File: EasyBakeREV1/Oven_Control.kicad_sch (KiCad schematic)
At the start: 11 parts, among them U6 SQ2310ES_SOT23, U9 SN74LVC1G32

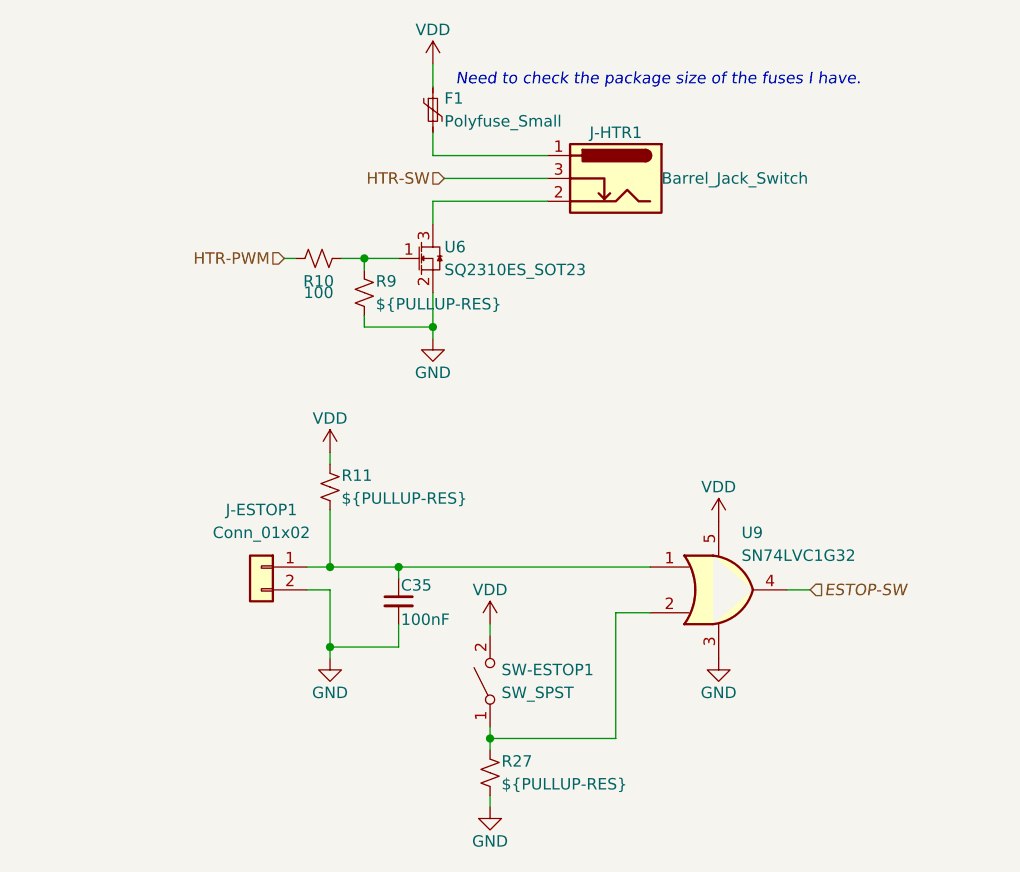
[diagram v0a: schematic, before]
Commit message: REV3 - Reorganize MC pinouts and add LED driver (WIP)
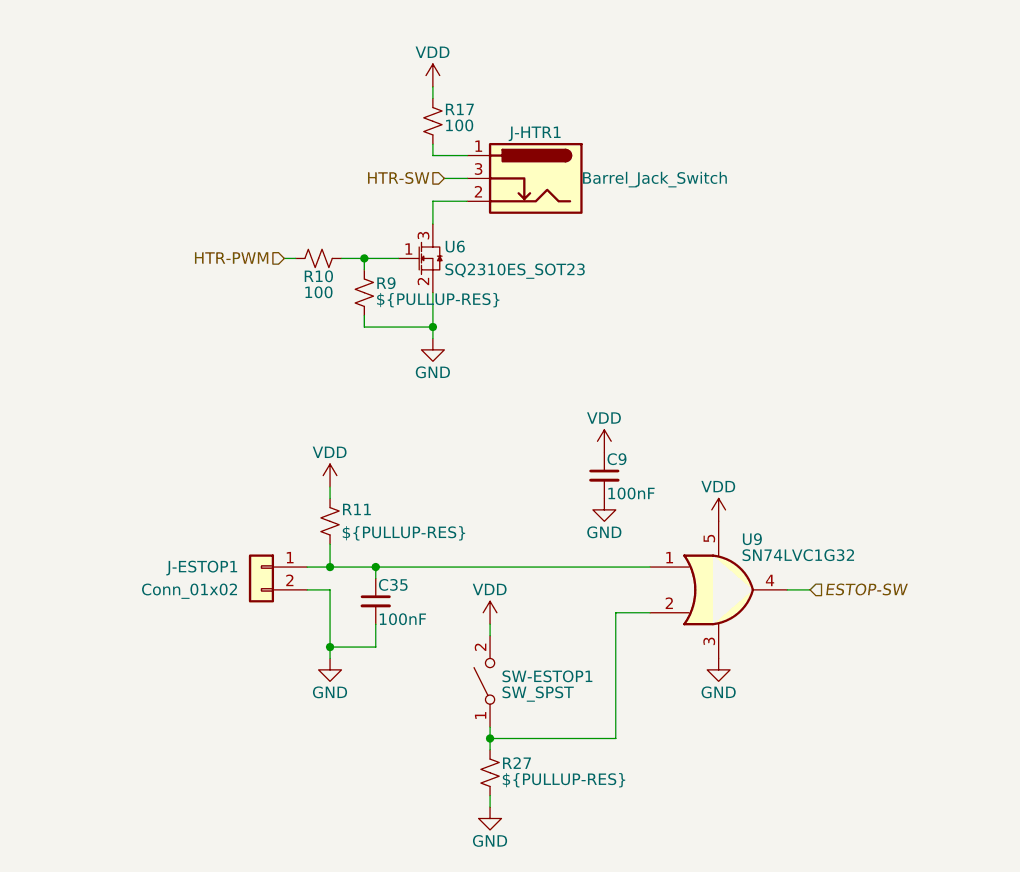
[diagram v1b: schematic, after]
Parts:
- removed F1: Polyfuse_Small, Fuse:Fuse_1210_3225Metric_Pad1.42x2.65mm_HandSolder, symbol Device:Polyfuse_Small
- added C9: 100nF, Capacitor_SMD:C_0603_1608Metric, symbol Device:C_Small
- added R17: 100, Resistor_SMD:R_0603_1608Metric, symbol Device:R_Small_US
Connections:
- net GND: now also C9.2
- net VDD: now also C9.1, R17.2
- net at J-HTR1.1: now also R17.1
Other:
- note removed: "Need to check the package size of the fuses I have."
- moved on the sheet: C35, J-HTR1, R11

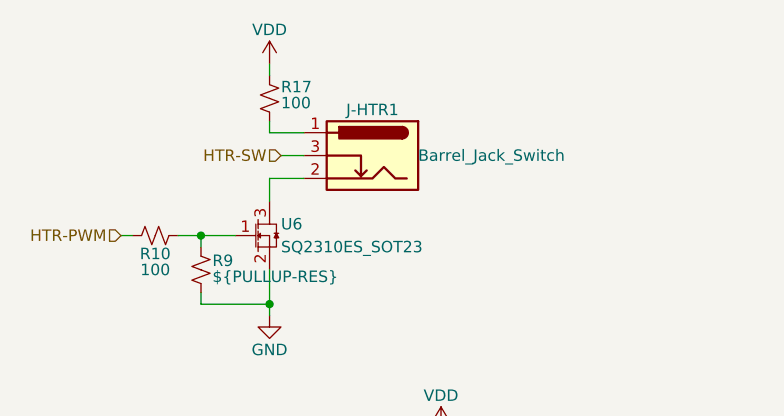
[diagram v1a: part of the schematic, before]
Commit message: Update to KiCad 7
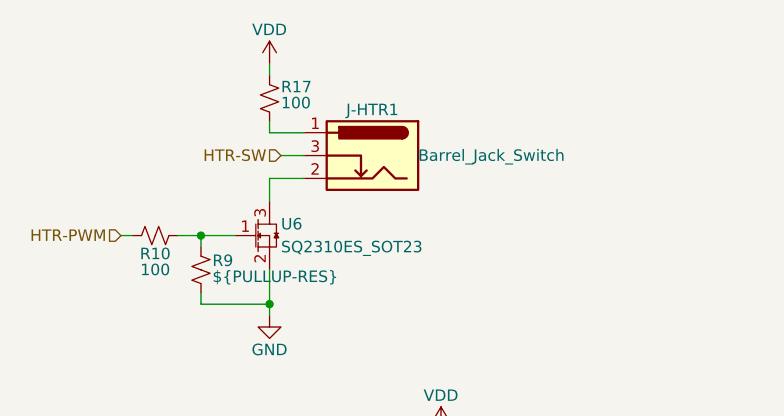
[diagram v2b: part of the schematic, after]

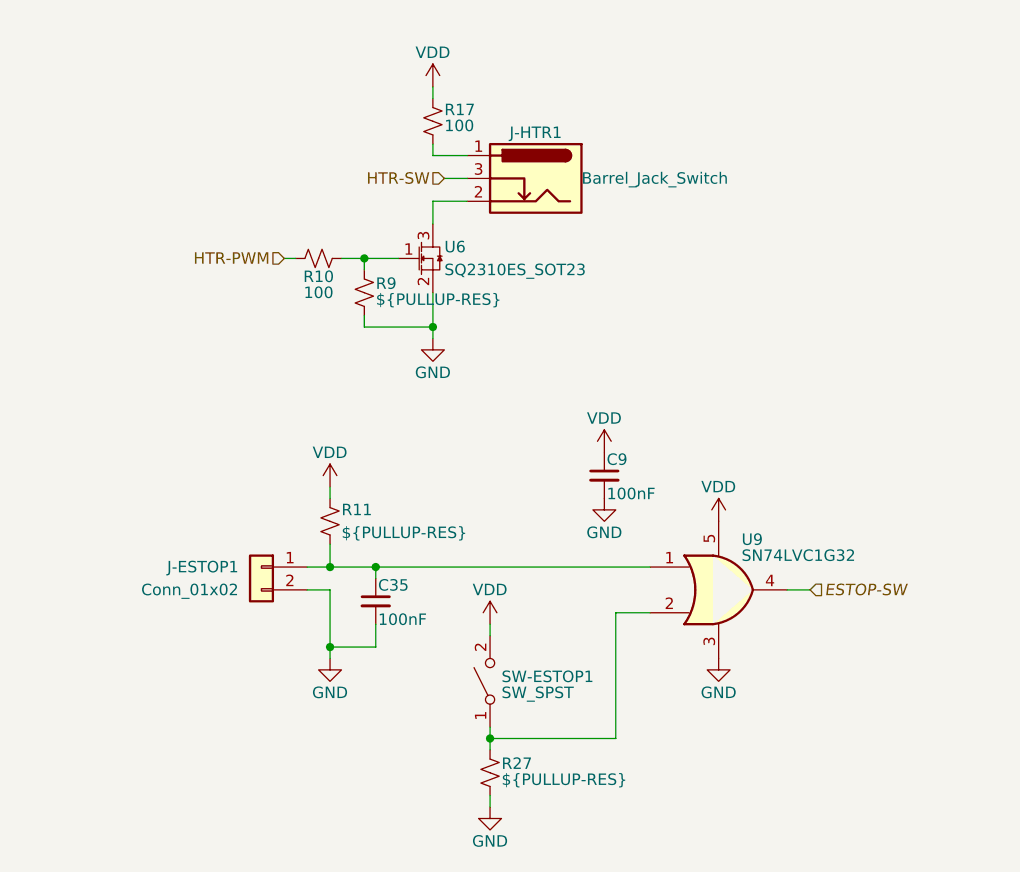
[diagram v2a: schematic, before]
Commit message: Change main pwr to 3.3 due to USB issues
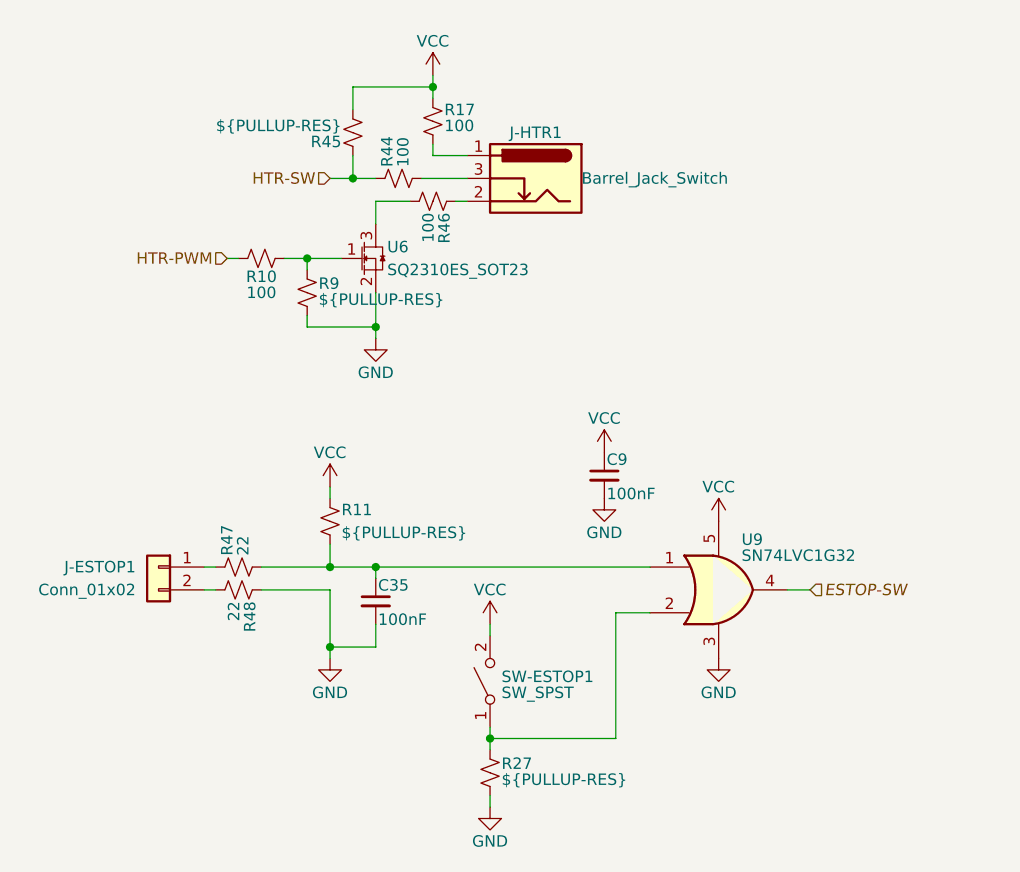
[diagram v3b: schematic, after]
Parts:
- added R44, R46: 100, Resistor_SMD:R_0603_1608Metric, symbol Device:R_Small_US
- added R45: ${PULLUP-RES}, Resistor_SMD:R_0603_1608Metric, symbol Device:R_Small_US
- added R47, R48: 22, Resistor_SMD:R_0603_1608Metric, symbol Device:R_Small_US
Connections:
- net GND: now also R48.2; no longer J-ESTOP1.2 (Pin_2)
- net HTR-SW: now also R44.2, R45.1; no longer J-HTR1.3
- net at C35.1, R11.1, U9.1: now also R47.1; no longer J-ESTOP1.1 (Pin_1)
- net at J-HTR1.2: now also R46.2; no longer U6.3 (D)
- net VDD renamed VCC
- net VCC: now also R45.2
- new net: J-HTR1.3, R44.1
- new net: J-ESTOP1.1 (Pin_1), R47.2
- new net: J-ESTOP1.2 (Pin_2), R48.1
- new net: R46.1, U6.3 (D)
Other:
- moved on the sheet: J-ESTOP1, R10, R9, U6

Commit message: Replaced MCU - started layout
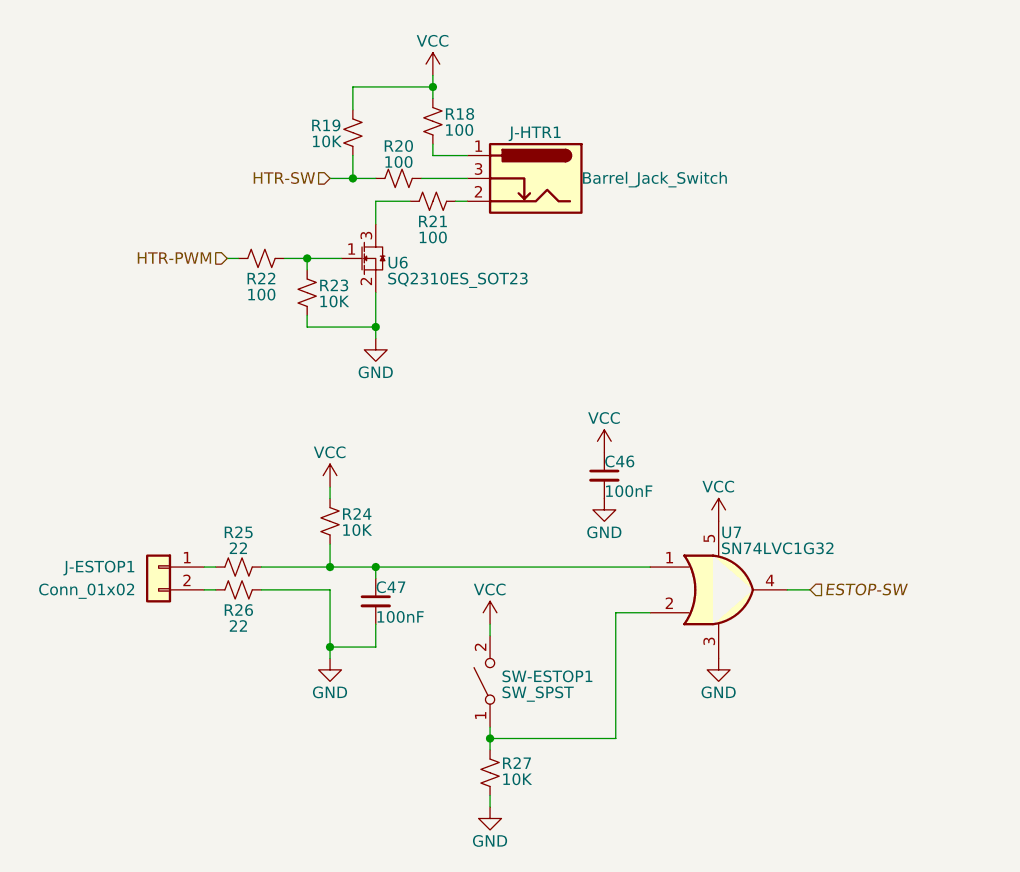
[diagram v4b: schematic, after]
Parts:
- C46: renamed from C9; footprint Capacitor_SMD:C_0603_1608Metric -> Capacitor_SMD:C_0402_1005Metric
- R18: renamed from R17; footprint Resistor_SMD:R_0603_1608Metric -> Resistor_SMD:R_0402_1005Metric
- R19: renamed from R45; value ${PULLUP-RES} -> 10K; footprint Resistor_SMD:R_0603_1608Metric -> Resistor_SMD:R_0402_1005Metric
- R20: renamed from R44; footprint Resistor_SMD:R_0603_1608Metric -> Resistor_SMD:R_0402_1005Metric
- R21: renamed from R46; footprint Resistor_SMD:R_0603_1608Metric -> Resistor_SMD:R_0402_1005Metric
- R22: renamed from R10; footprint Resistor_SMD:R_0603_1608Metric -> Resistor_SMD:R_0402_1005Metric
- R23: renamed from R9; value ${PULLUP-RES} -> 10K; footprint Resistor_SMD:R_0603_1608Metric -> Resistor_SMD:R_0402_1005Metric
- R24: renamed from R11; value ${PULLUP-RES} -> 10K; footprint Resistor_SMD:R_0603_1608Metric -> Resistor_SMD:R_0402_1005Metric
- R25: renamed from R47; footprint Resistor_SMD:R_0603_1608Metric -> Resistor_SMD:R_0402_1005Metric
- R26: renamed from R48; footprint Resistor_SMD:R_0603_1608Metric -> Resistor_SMD:R_0402_1005Metric
- R27: value ${PULLUP-RES} -> 10K; footprint Resistor_SMD:R_0603_1608Metric -> Resistor_SMD:R_0402_1005Metric
- renumbered C35 to C47, U9 to U7

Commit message: Rearrange footprints and start layout
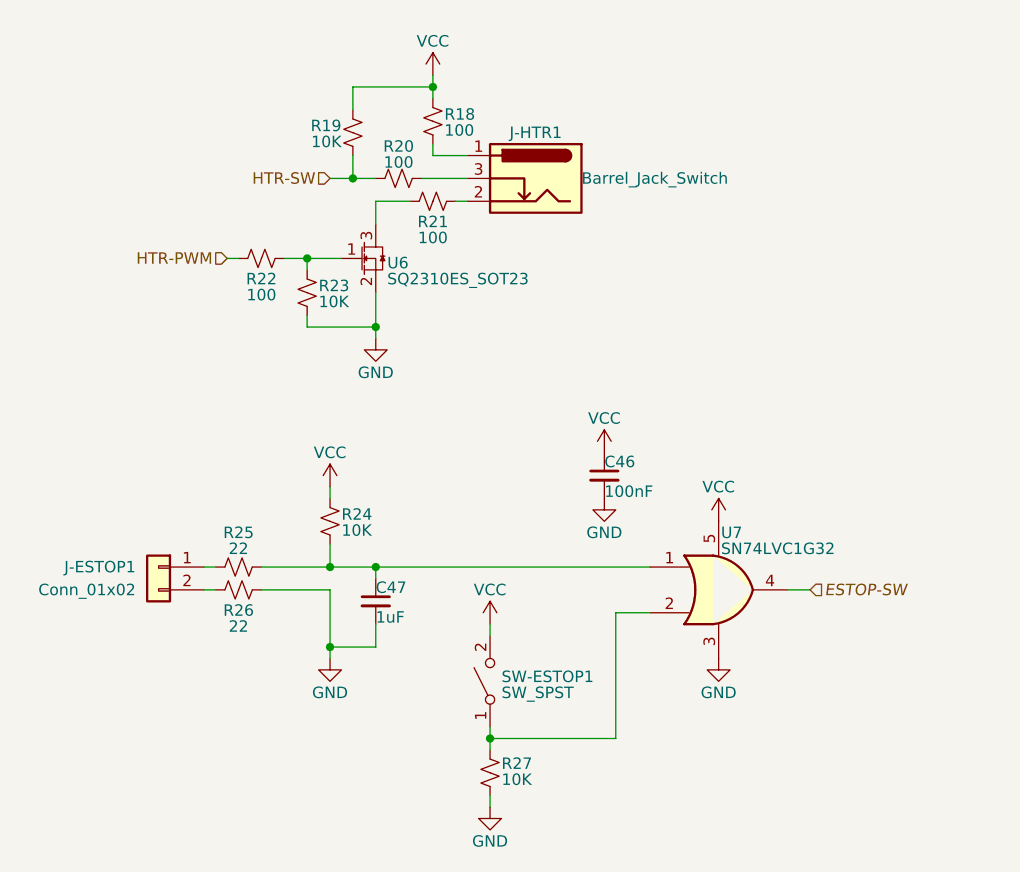
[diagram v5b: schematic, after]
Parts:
- C47: value 100nF -> 1uF
- J-HTR1: footprint Connector_BarrelJack:BarrelJack_Horizontal -> Daxxn_Connectors:BarrelJack_Horizontal
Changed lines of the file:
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@@
       (effects (font (size 1.27 1.27)) (justify left))
     )
-    (property "Value" "100nF" (at 53.34 84.328 0)
+    (property "Value" "1uF" (at 53.34 84.328 0)
       (effects (font (size 1.27 1.27)) (justify left))
     )
@@
     )
     (property "Datasheet" "~" (at 53.34 82.55 0)
+      (effects (font (size 1.27 1.27)) hide)
+    )
+    (property "Schematic" "" (at 53.34 82.55 0)
+      (effects (font (size 1.27 1.27)) hide)
+    )
+    (property "PartNumber" "" (at 53.34 82.55 0)
+      (effects (font (size 1.27 1.27)))
+    )
+    (property "SupplierPN" "" (at 53.34 82.55 0)
       (effects (font (size 1.27 1.27)) hide)
     )
@@
       (effects (font (size 1.27 1.27)) (justify right))
     )
-    (property "Footprint" "Connector_BarrelJack:BarrelJack_Horizontal" (at 69.85 36.576 0)
+    (property "Footprint" "Daxxn_Connectors:BarrelJack_Horizontal" (at 69.85 36.576 0)
       (effects (font (size 1.27 1.27)) hide)
     )
@@
       (effects (font (size 1.27 1.27)) hide)
     )
+    (property "Schematic" "" (at 71.12 35.56 0)
+      (effects (font (size 1.27 1.27)) hide)
+    )
+    (property "PartNumber" "" (at 71.12 35.56 0)
+      (effects (font (size 1.27 1.27)))
+    )
+    (property "SupplierPN" "" (at 71.12 35.56 0)
+      (effects (font (size 1.27 1.27)) hide)
+    )
